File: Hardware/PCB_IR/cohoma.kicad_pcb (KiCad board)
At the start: 2 copper layers, 32.9 x 32.6 mm, 11 parts, among them J2 Conn_01x03, U1 MCP2120-I/P, U2 TSOP75338WTT, Y1 ABLS-7.3728MHz-20-B-3-H-T

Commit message: version finale
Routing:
- net Q_OUT: track 21.6 -> 20.0 mm
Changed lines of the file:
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@@
     (property "ki_keywords" "cap capacitor")
     (attr smd)
-    (fp_text reference "C3" (at 0 -3.2) (layer "F.SilkS")
+    (fp_text reference "C3" (at 3.24 -2.14) (layer "F.SilkS")
         (effects (font (size 1 1) (thickness 0.15)))
     )
@@
     (property "ki_keywords" "cap capacitor")
     (attr smd)
-    (fp_text reference "C1" (at 0 -3.2) (layer "F.SilkS")
+    (fp_text reference "C1" (at -3.74 -1.78) (layer "F.SilkS")
         (effects (font (size 1 1) (thickness 0.15)))
     )
@@
     (property "ki_keywords" "cap capacitor")
     (attr smd)
-    (fp_text reference "C2" (at -1.195563 -2.26) (layer "F.SilkS")
+    (fp_text reference "C2" (at 0.83 -3.82) (layer "F.SilkS")
         (effects (font (size 1 1) (thickness 0.15)))
     )
@@
   (segment (start 131.19 89.95) (end 131.19 79.73) (width 0.5) (layer "B.Cu") (net 2))
   (segment (start 134.73 71.85) (end 134.73 73.91) (width 0.3) (layer "F.Cu") (net 3))
-  (segment (start 129.04 79.6) (end 127.45 79.6) (width 0.3) (layer "F.Cu") (net 3))
   (segment (start 136.28 67.46) (end 136.28 70.3) (width 0.3) (layer "F.Cu") (net 3))
   (segment (start 134.73 73.91) (end 129.04 79.6) (width 0.3) (layer "F.Cu") (net 3))
@@
   (segment (start 124.27 73.97) (end 123.35 73.05) (width 0.5) (layer "B.Cu") (net 4))
   (segment (start 129.47 73.97) (end 124.27 73.97) (width 0.5) (layer "B.Cu") (net 4))
-  (segment (start 127.505 76.785) (end 127.57 76.85) (width 0.5) (layer "B.Cu") (net 4))
   (zone (net 2) (net_name "GND") (layer "F.Cu") (hatch edge 0.5)
     (connect_pads (clearance 0.5))

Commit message: Version vraiment finale
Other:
- board text added: "B"
- board text added: "MAËNA CHARBONNIER"
- board text added: "T"
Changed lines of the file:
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@@
   (gr_arc (start 120 93.55) (mid 115.947004 91.684798) (end 114.4 87.5)
     (stroke (width 0.05) (type default)) (layer "Edge.Cuts"))
+  (gr_text "MAËNA CHARBONNIER" (at 126.93 92.16) (layer "F.Cu")
+    (effects (font (size 1 1) (thickness 0.15)) (justify left bottom))
+  )
+  (gr_text "T" (at 145.1 83.71) (layer "F.Cu")
+    (effects (font (size 1 1) (thickness 0.15)) (justify left bottom))
+  )
+  (gr_text "B" (at 145.26 86.43) (layer "B.Cu")
+    (effects (font (size 1 1) (thickness 0.15)) (justify left bottom))
+  )
   (segment (start 128.3 78.365) (end 127.225 78.365) (width 0.3) (layer "F.Cu") (net 1))
   (segment (start 127.225 78.365) (end 127.075 78.215) (width 0.3) (layer "F.Cu") (net 1))

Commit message: pcb
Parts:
- C1, C2, C3: footprint Capacitor_SMD:CP_Elec_4x5.4 -> Capacitor_SMD:C_0201_0603Metric_Pad0.64x0.40mm_HandSolder
- U1: footprint Package_SO:SOIC-8-N7_3.9x4.9mm_P1.27mm -> Package_SO:SOIC-14_3.9x8.7mm_P1.27mm
- U2: footprint Capacitor_SMD:CP_Elec_4x5.4 -> Package_SO:TSOP753TT
- moved U2 103.1 mm to (243.7, 86.5)
- moved C2 9.29 mm to (124.6, 80.4)
- moved H2 5.34 mm to (141.5, 82.2)
- moved H4 5.34 mm to (120.0, 82.2)
- moved Y1 4.46 mm to (130.6, 66.3)
- moved U1 3.20 mm to (130.7, 75.8)
- moved J2 3.19 mm to (121.8, 76.1)
- moved C3 1.81 mm to (133.3, 62.8)
- moved C1 1.30 mm to (127.0, 62.7)
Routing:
- net +3.3V: track 104.0 -> 25.7 mm, vias 2 -> 3
- net GND: track 78.7 -> 2.48 mm, vias 2 -> 0
- net UART_RX: track 0.00 -> 17.4 mm
- net Q_IN: track 17.4 -> 14.3 mm
- net Q_OUT: track 20.0 -> 20.8 mm
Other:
- board size 32.9 x 32.6 mm -> 33.3 x 26.3 mm

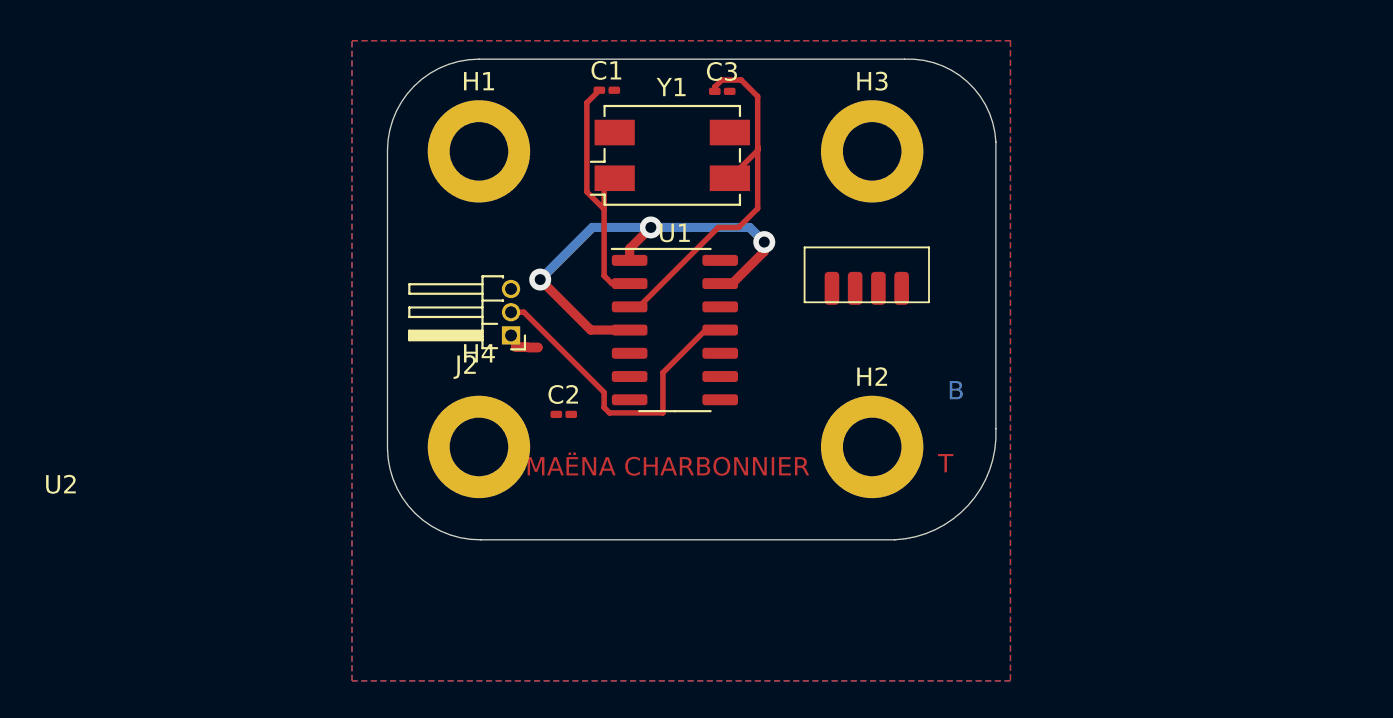
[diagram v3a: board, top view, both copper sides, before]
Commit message: pcb sans erreurs (mais avec track à 0.3)
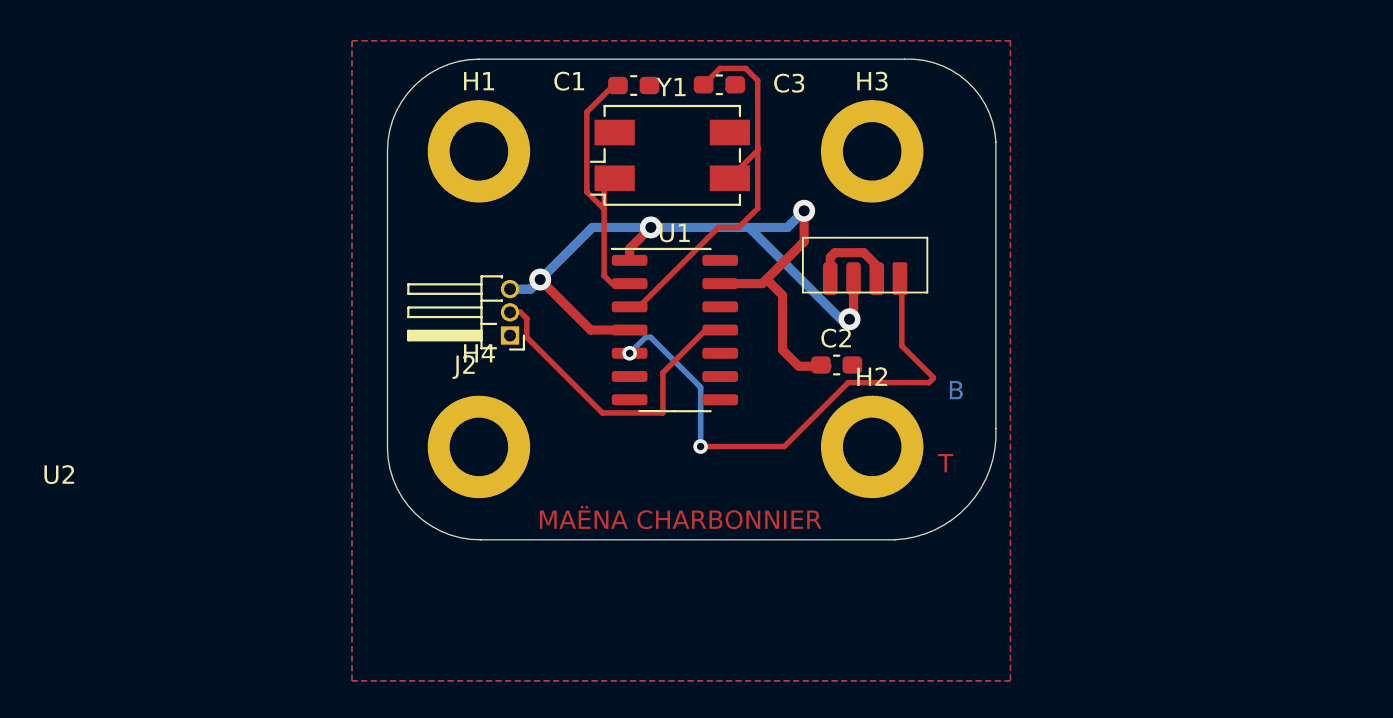
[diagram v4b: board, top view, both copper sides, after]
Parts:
- C1, C2, C3: footprint Capacitor_SMD:C_0201_0603Metric_Pad0.64x0.40mm_HandSolder -> Capacitor_SMD:C_0603_1608Metric_Pad1.08x0.95mm_HandSolder
- moved C2 15.2 mm to (139.6, 77.7)
- moved C1 1.49 mm to (128.5, 62.4)
- moved U2 0.54 mm to (243.6, 86.0)
- moved C3 0.39 mm to (133.1, 62.4)
- moved J2 0.06 mm to (121.7, 76.1)
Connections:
- U2 pad GND: (no net) -> GND
- U2 pad OUT: (no net) -> RXIR
- U2 pad VS: (no net) -> +3.3V
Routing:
- net RXIR: track 0.00 -> 29.4 mm, vias 0 -> 2
- net +3.3V: track 25.7 -> 50.3 mm, vias 3 -> 4
- net GND: track 2.48 -> 4.82 mm
- net Q_OUT: track 20.8 -> 22.2 mm
- net Q_IN: track 14.3 -> 15.1 mm

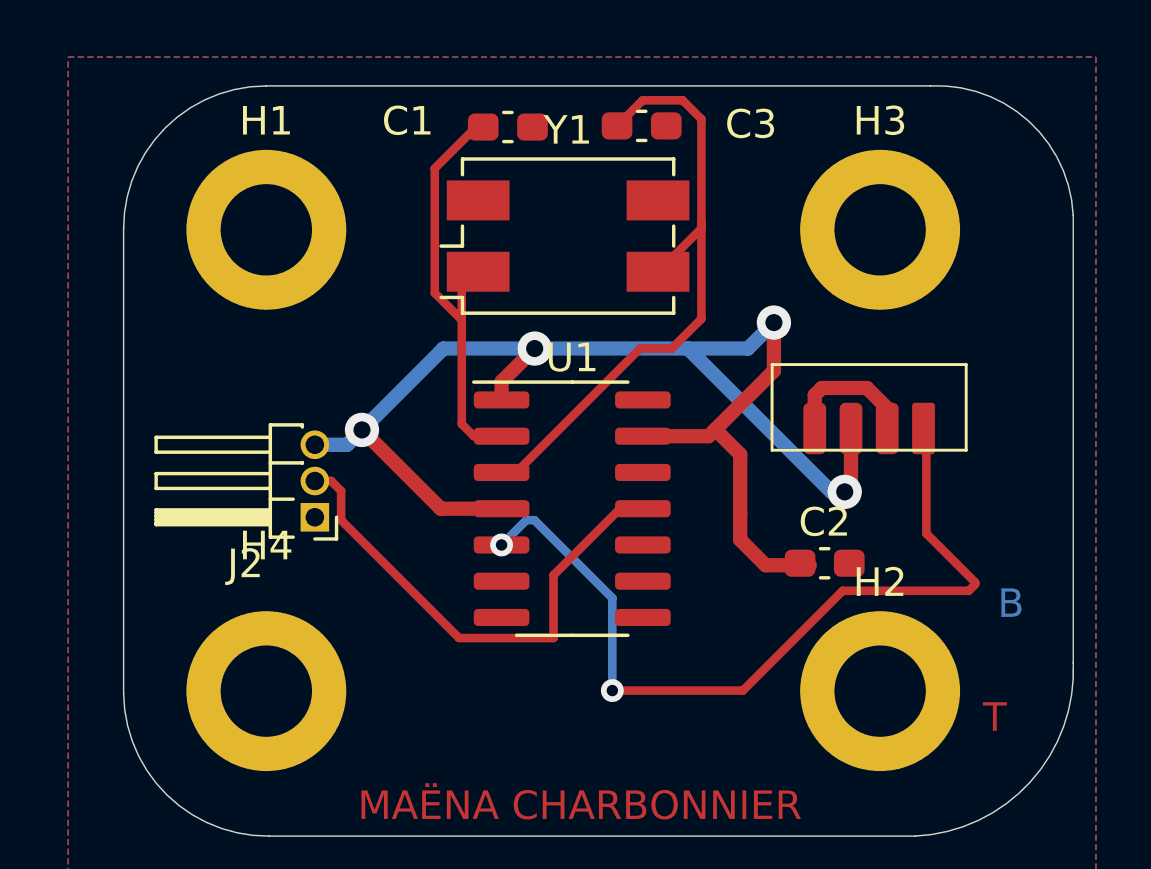
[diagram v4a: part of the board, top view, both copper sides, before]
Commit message: pcb avec tracks à 5 mm
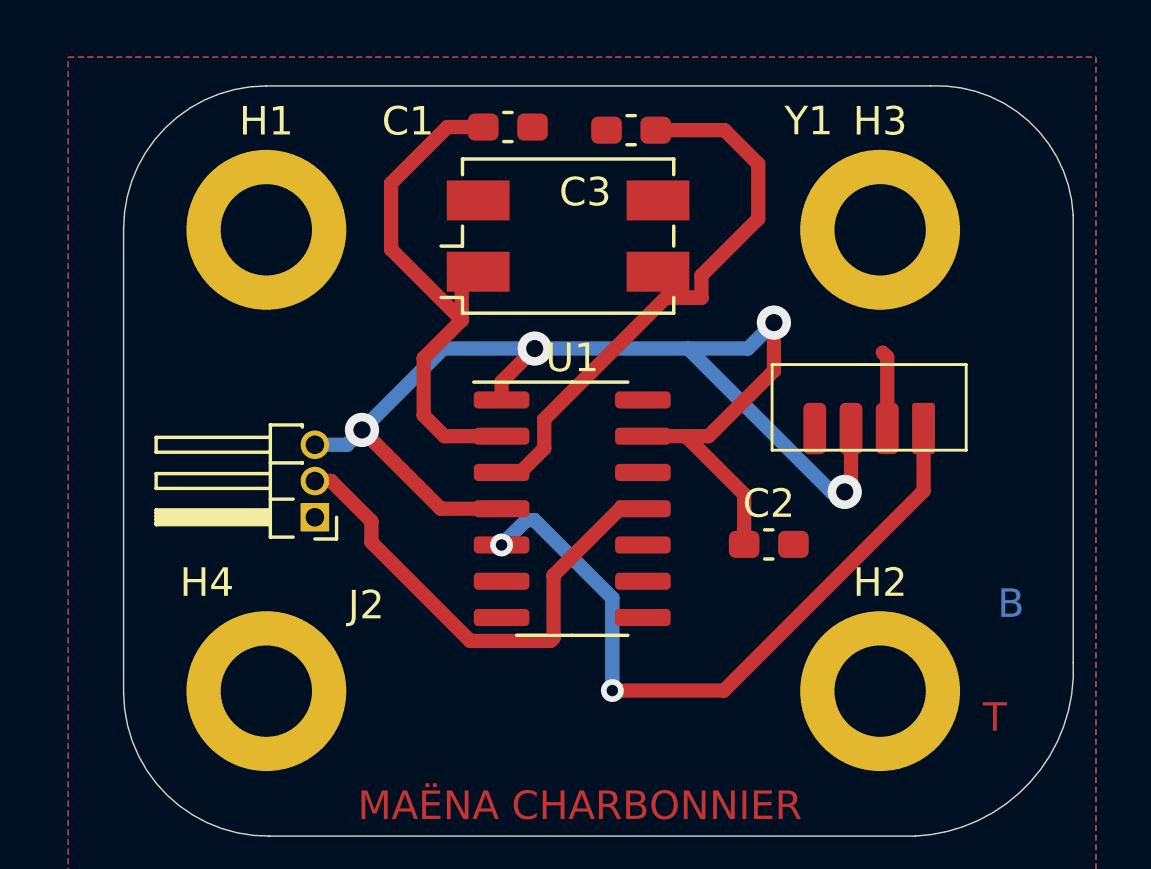
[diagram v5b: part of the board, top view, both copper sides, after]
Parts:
- moved C2 2.07 mm to (137.6, 77.1)
- moved C3 0.40 mm to (132.8, 62.5), turned to 180 degrees
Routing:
- net RXIR: track 29.4 -> 24.6 mm
- net Q_IN: track 15.1 -> 18.7 mm
- net +3.3V: track 50.3 -> 47.9 mm
- net GND: track 4.82 -> 2.73 mm
- net Q_OUT: track 22.2 -> 21.6 mm

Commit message: pcb fini
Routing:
- net RXIR: track 24.6 -> 26.3 mm
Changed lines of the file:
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@@
   (segment (start 135.49 73.27) (end 134.7 73.27) (width 0.5) (layer "F.Cu") (net 4))
   (segment (start 136.7375 77.06) (end 136.7375 75.3075) (width 0.5) (layer "F.Cu") (net 4))
-  (via (at 123.35 73.05) (size 1.2) (drill 0.6) (layers "F.Cu" "B.Cu") (net 4))
-  (via (at 140.26 75.22) (size 1.2) (drill 0.6) (layers "F.Cu" "B.Cu") (net 4))
-  (via (at 129.4 70.2) (size 1.2) (drill 0.6) (layers "F.Cu" "B.Cu") (net 4))
-  (via (at 137.78 69.29) (size 1.2) (drill 0.6) (layers "F.Cu" "B.Cu") (net 4))
+  (via (at 123.35 73.05) (size 1.6) (drill 0.8) (layers "F.Cu" "B.Cu") (net 4))
+  (via (at 140.26 75.22) (size 1.6) (drill 0.8) (layers "F.Cu" "B.Cu") (net 4))
+  (via (at 129.4 70.2) (size 1.6) (drill 0.8) (layers "F.Cu" "B.Cu") (net 4))
+  (via (at 137.78 69.29) (size 1.6) (drill 0.8) (layers "F.Cu" "B.Cu") (net 4))
   (segment (start 140.26 75.22) (end 139.79 75.22) (width 0.5) (layer "B.Cu") (net 4))
   (segment (start 126.2 70.2) (end 123.35 73.05) (width 0.5) (layer "B.Cu") (net 4))
@@
   (segment (start 121.7 73.57) (end 122.83 73.57) (width 0.5) (layer "B.Cu") (net 4))
   (segment (start 134.77 70.2) (end 129.4 70.2) (width 0.5) (layer "B.Cu") (net 4))
+  (segment (start 128.24 77.08) (end 129.12 77.08) (width 0.5) (layer "F.Cu") (net 5))
   (segment (start 143.02 73) (end 143.02 75.19) (width 0.5) (layer "F.Cu") (net 5))
   (segment (start 143.02 75.19) (end 136.03 82.18) (width 0.5) (layer "F.Cu") (net 5))
+  (segment (start 129.12 77.08) (end 130.67 75.53) (width 0.5) (layer "F.Cu") (net 5))
   (segment (start 136.03 82.18) (end 132.12 82.18) (width 0.5) (layer "F.Cu") (net 5))
-  (via (at 132.12 82.18) (size 0.8) (drill 0.4) (layers "F.Cu" "B.Cu") (net 5))
-  (via (at 128.24 77.08) (size 0.8) (drill 0.4) (layers "F.Cu" "B.Cu") (net 5))
-  (segment (start 129.11 76.21) (end 128.24 77.08) (width 0.5) (layer "B.Cu") (net 5))
-  (segment (start 129.39 76.21) (end 129.11 76.21) (width 0.5) (layer "B.Cu") (net 5))
-  (segment (start 132.12 78.94) (end 129.39 76.21) (width 0.5) (layer "B.Cu") (net 5))
-  (segment (start 132.12 82.18) (end 132.12 78.94) (width 0.5) (layer "B.Cu") (net 5))
+  (via (at 132.12 82.18) (size 1.6) (drill 0.8) (layers "F.Cu" "B.Cu") (net 5))
+  (via (at 130.67 75.53) (size 1.6) (drill 0.8) (layers "F.Cu" "B.Cu") (net 5))
+  (segment (start 132.12 78.94) (end 132.12 82.18) (width 0.5) (layer "B.Cu") (net 5))
+  (segment (start 130.67 77.49) (end 132.12 78.94) (width 0.5) (layer "B.Cu") (net 5))
+  (segment (start 130.67 75.53) (end 130.67 77.49) (width 0.5) (layer "B.Cu") (net 5))
   (segment (start 127.137477 80.44) (end 129.96 80.44) (width 0.5) (layer "F.Cu") (net 7))
   (segment (start 123.68 76.982523) (end 127.137477 80.44) (width 0.5) (layer "F.Cu") (net 7))

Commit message: final
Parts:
- Y1: footprint Crystal:Crystal_SMD_EuroQuartz_MQ-4Pin_7.0x5.0mm -> Crystal:Crystal_SMD_7050-2Pin_7.0x5.0mm
- moved C3 0.32 mm to (132.8, 62.2)
- moved Y1 0.30 mm to (130.8, 66.1)
- moved C1 0.17 mm to (128.4, 62.3)
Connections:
- U2 pad GND: GND -> (no net)
- U2 pad OUT: RXIR -> (no net)
- U2 pad VS: +3.3V -> (no net)
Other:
- board text added: "IR"
- board text removed: "MAËNA CHARBONNIER"
